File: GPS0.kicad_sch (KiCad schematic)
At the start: 12 parts, among them J2 GPS_ANT_0, U3 NEO-6M-GPS

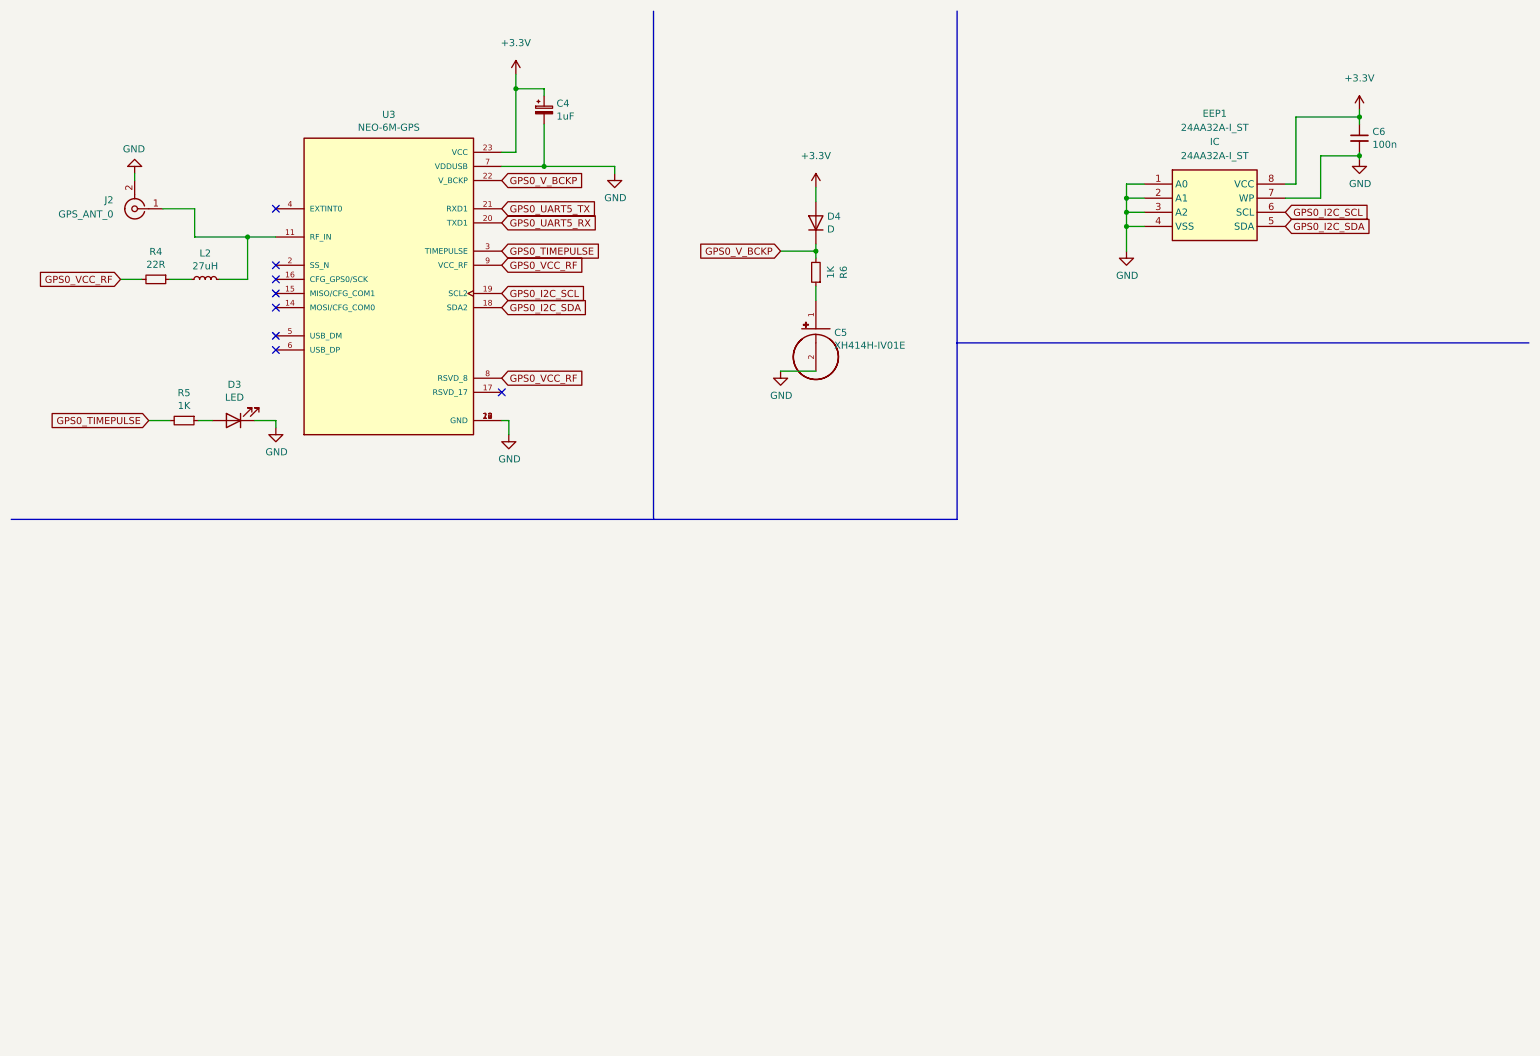
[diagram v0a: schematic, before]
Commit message: Adding M10
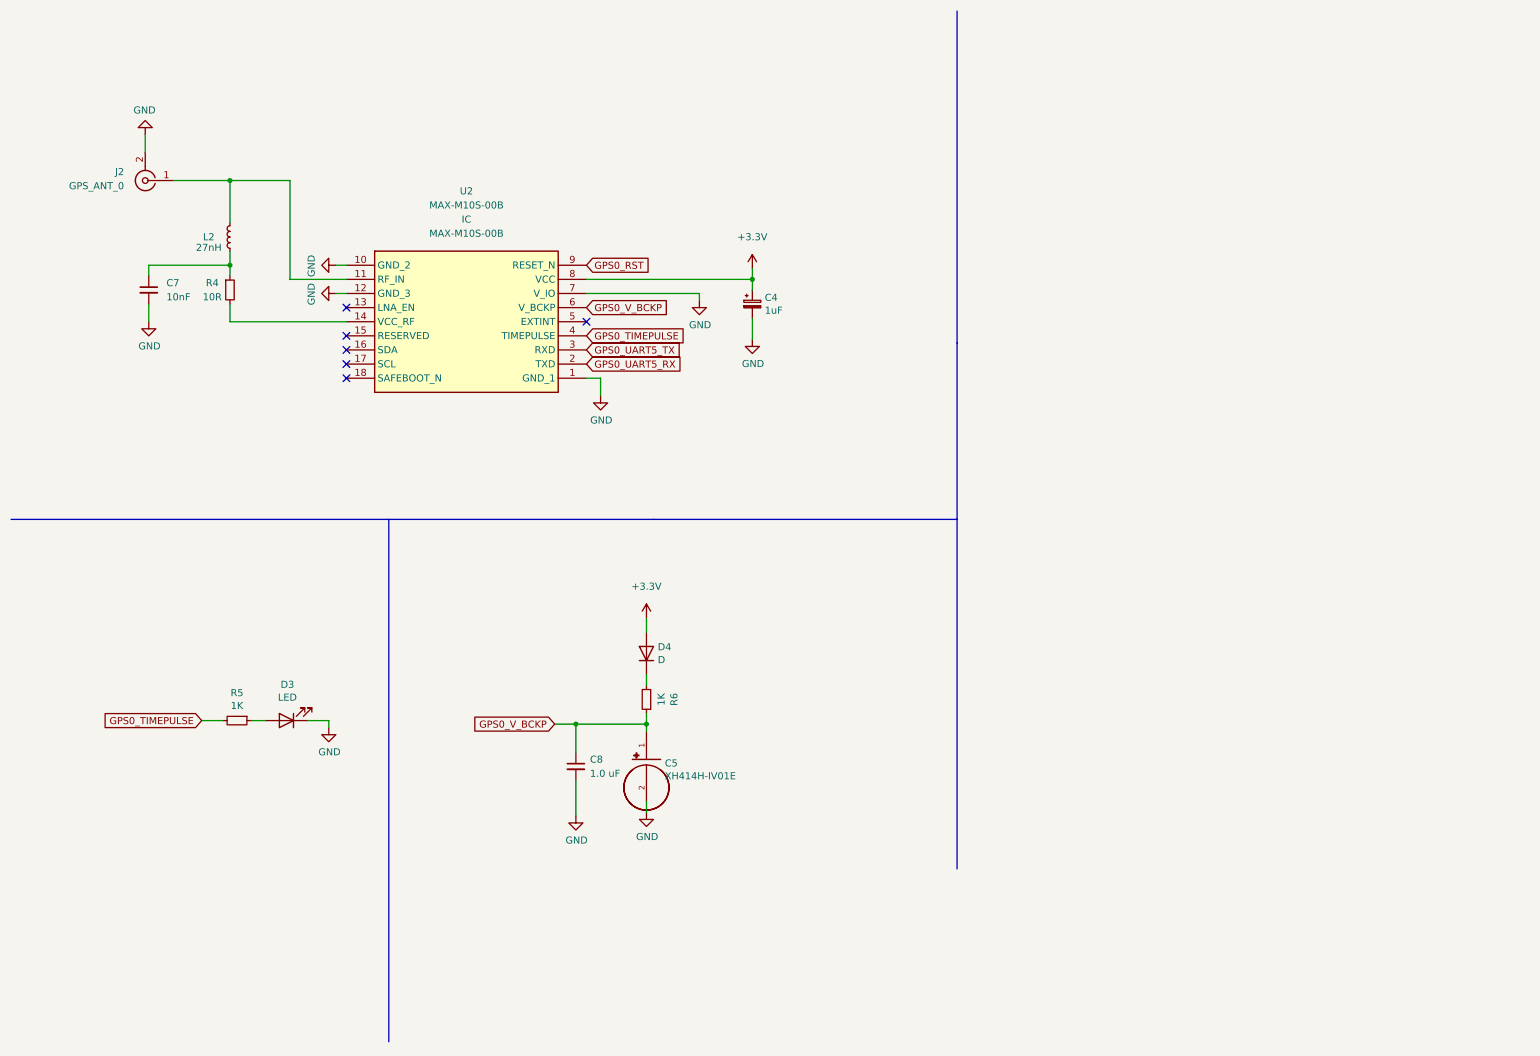
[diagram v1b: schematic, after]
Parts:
- removed C6: 100n, Capacitor_SMD:C_0402_1005Metric, symbol Device:C_Small
- removed EEP1: 24AA32A-I_ST, 24AA32A-I_ST:SOP65P640X120-8N, symbol 24AA32A-I_ST:24AA32A-I_ST
- removed U3: NEO-6M-GPS, NEO 6M:XCVR_NEO-6M-GPS, symbol NEO-6M-GPS:NEO-6M-GPS
- added C7: 10nF, Capacitor_SMD:C_0805_2012Metric, symbol Device:C_Small
- added C8: 1.0 uF, Capacitor_SMD:C_0805_2012Metric, symbol Device:C_Small
- added U2: MAX-M10S-00B, MAX-M10S-00B:MAXM10S00B, symbol MAX-M10S-00B:MAX-M10S-00B
- L2: value 27uH -> 27nH
- R4: value 22R -> 10R
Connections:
- net +3.3V: now also U2.8 (VCC)
- net GND: now also C7.2, C8.2, U2.1 (GND_1), U2.10 (GND_2), U2.12 (GND_3), U2.7 (V_IO)
- net GPS0_TIMEPULSE: now also U2.4 (TIMEPULSE)
- net GPS0_UART5_RX: now also U2.2 (TXD)
- net GPS0_UART5_TX: now also U2.3 (RXD)
- net GPS0_V_BCKP: now also C5.1, R6.1, C8.1, U2.6 (V_BCKP); no longer D4.1 (K), R6.2
- net at J2.1 (In), L2.2: now also U2.11 (RF_IN)
- net at L2.1, R4.1: now also C7.1
- net GPS0_VCC_RF: no longer names the net of R4.2
- net GPS0_VCC_RF: now also U2.14 (VCC_RF)
- new net: D4.1 (K), R6.2
- new net GPS0_RST: U2.9 (RESET_N)
- no-connect marks 8 -> 6
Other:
- moved on the sheet: C4, C5, D3, D4, J2, L2, R4, R5, R6

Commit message: Finished M10
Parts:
- C7: footprint Capacitor_SMD:C_0805_2012Metric -> Capacitor_SMD:C_0402_1005Metric
- L2: footprint Inductor_SMD:L_0805_2012Metric -> Inductor_SMD:L_0402_1005Metric
- R4: footprint Resistor_SMD:R_0805_2012Metric -> Resistor_SMD:R_0402_1005Metric
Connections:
- net GPS0_RST renamed GPS0_RESET
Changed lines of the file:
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@@
     )
   )
-  (global_label "GPS0_RST" (shape input) (at 115.57 57.785 0) (fields_autoplaced)
+  (global_label "GPS0_RESET" (shape input) (at 115.57 57.785 0) (fields_autoplaced)
     (effects (font (size 1.27 1.27)) (justify left))
-    (property "Intersheet References" "${INTERSHEET_REFS}" (id 0) (at 127.3569 57.7056 0)
+    (property "Intersheet References" "${INTERSHEET_REFS}" (id 0) (at 129.655 57.7056 0)
       (effects (font (size 1.27 1.27)) (justify left) hide)
     )
@@
     (property "Reference" "L2" (id 0) (at 47.625 52.705 0))
     (property "Value" "27nH" (id 1) (at 47.625 54.61 0))
-    (property "Footprint" "Inductor_SMD:L_0805_2012Metric" (id 2) (at 51.435 52.705 0)
+    (property "Footprint" "Inductor_SMD:L_0402_1005Metric" (id 2) (at 51.435 52.705 0)
       (effects (font (size 1.27 1.27)) hide)
     )
@@
       (effects (font (size 1.27 1.27)) (justify left))
     )
-    (property "Footprint" "Capacitor_SMD:C_0805_2012Metric" (id 2) (at 36.83 62.23 0)
+    (property "Footprint" "Capacitor_SMD:C_0402_1005Metric" (id 2) (at 36.83 62.23 0)
       (effects (font (size 1.27 1.27)) hide)
     )
@@
     (property "Reference" "R4" (id 0) (at 48.26 60.96 0))
     (property "Value" "10R" (id 1) (at 48.26 63.5 0))
-    (property "Footprint" "Resistor_SMD:R_0805_2012Metric" (id 2) (at 51.435 62.23 0)
-      (effects (font (size 1.27 1.27)) hide)
-    )
+    (property "Footprint" "Resistor_SMD:R_0402_1005Metric" (id 2) (at 51.435 62.23 0)
+      (effects (font (size 1.27 1.27)) hide)
+    )

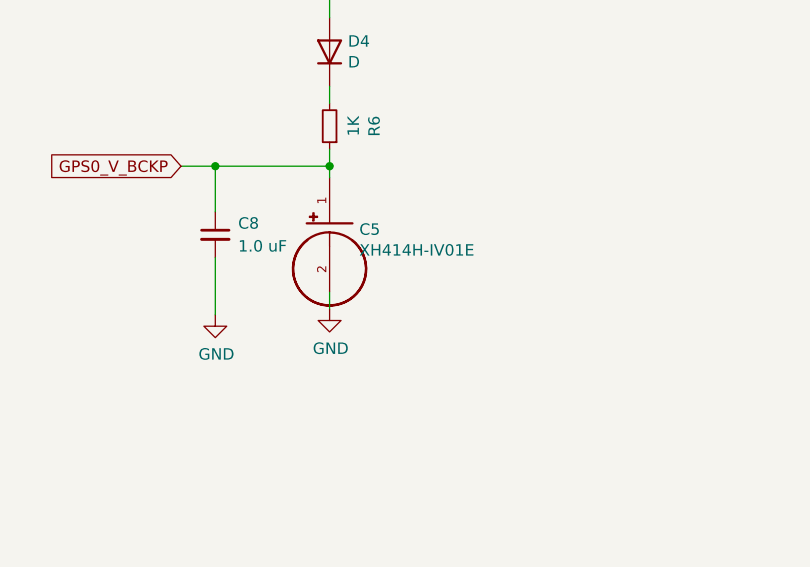
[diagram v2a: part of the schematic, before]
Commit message: Corrected battery position
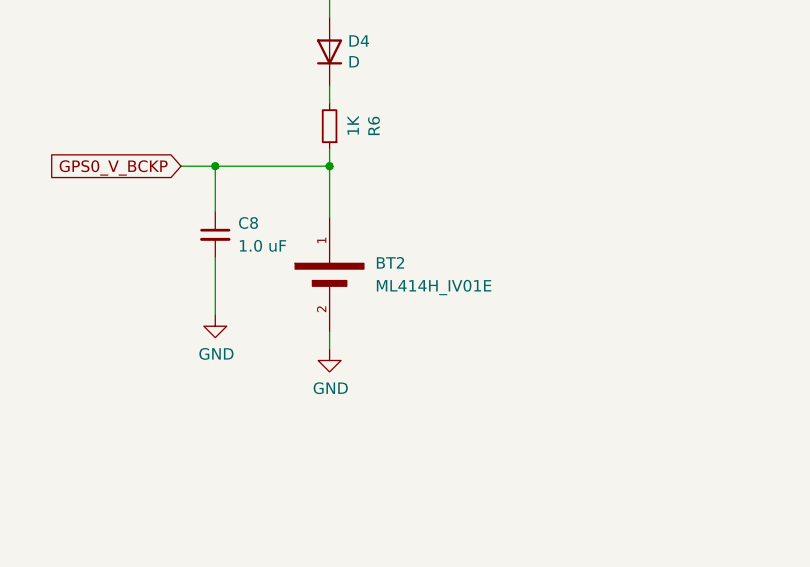
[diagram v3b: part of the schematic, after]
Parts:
- removed C5: XH414H-IV01E, XH414H:CAP_XH414H-IV01E, symbol XH414H-IV01E:XH414H-IV01E
- added BT2: ML414H_IV01E, ML414H_IV01E:SEIKO_ML414H_IV01E, symbol ML414H_IV01E:ML414H_IV01E
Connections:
- net GND: now also BT2.2
- net GPS0_V_BCKP: now also BT2.1
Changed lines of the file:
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@@
     (stroke (width 0) (type default) (color 0 0 0 0))
   )
-  (wire (pts (xy 126.365 154.305) (xy 126.365 156.21))
+  (wire (pts (xy 126.365 158.75) (xy 126.365 160.655))
     (stroke (width 0) (type default) (color 0 0 0 0))
   )
@@
     (stroke (width 0) (type default) (color 0 0 0 0))
   )
-  (wire (pts (xy 126.365 140.335) (xy 126.365 141.605))
+  (wire (pts (xy 126.365 140.335) (xy 126.365 146.05))
     (stroke (width 0) (type default) (color 0 0 0 0))
   )
@@
     (pin "2")
   )
-  (symbol (lib_id "XH414H-IV01E:XH414H-IV01E") (at 126.365 146.685 0) (unit 1)
-    (in_bom yes) (on_board yes)
-    (property "Reference" "C5" (id 0) (at 129.667 147.3708 0)
-      (effects (font (size 1.27 1.27)) (justify left))
-    )
-    (property "Value" "XH414H-IV01E" (id 1) (at 129.667 149.6822 0)
-      (effects (font (size 1.27 1.27)) (justify left))
-    )
-    (property "Footprint" "XH414H:CAP_XH414H-IV01E" (id 2) (at 126.365 146.685 0)
-      (effects (font (size 1.27 1.27)) (justify left bottom) hide)
-    )
-    (property "Datasheet" "" (id 3) (at 126.365 146.685 0)
-      (effects (font (size 1.27 1.27)) (justify left bottom) hide)
-    )
-    (property "MANUFACTURER" "Seiko" (id 4) (at 126.365 146.685 0)
-      (effects (font (size 1.27 1.27)) (justify left bottom) hide)
-    )
-    (pin "1")
-    (pin "2")
-  )
   (symbol (lib_id "Device:L_Small") (at 51.435 52.705 180) (unit 1)
     (in_bom yes) (on_board yes)
@@
     (pin "1")
   )
+  (symbol (lib_id "ML414H_IV01E:ML414H_IV01E") (at 126.365 151.13 270) (unit 1)
+    (in_bom yes) (on_board yes) (fields_autoplaced)
+    (property "Reference" "BT2" (id 0) (at 131.445 151.1299 90)
+      (effects (font (size 1.27 1.27)) (justify left))
+    )
+    (property "Value" "ML414H_IV01E" (id 1) (at 131.445 153.6699 90)
+      (effects (font (size 1.27 1.27)) (justify left))
+    )
+    (property "Footprint" "ML414H_IV01E:SEIKO_ML414H_IV01E" (id 2) (at 126.365 151.13 0)
+      (effects (font (size 1.27 1.27)) (justify bottom) hide)
+    )
+    (property "Datasheet" "" (id 3) (at 126.365 151.13 0)
+      (effects (font (size 1.27 1.27)) hide)
+    )
+    (property "STANDARD" "Manufacturer Recommendation" (id 4) (at 126.365 151.13 0)
+      (effects (font (size 1.27 1.27)) (justify bottom) hide)
+    )
+    (property "MANUFACTURER" "SEIKO" (id 5) (at 126.365 151.13 0)
+      (effects (font (size 1.27 1.27)) (justify bottom) hide)
+    )
+    (pin "1")
+    (pin "2")
+  )
   (symbol (lib_id "power:GND") (at 135.89 64.135 0) (unit 1)
     (in_bom yes) (on_board yes)
@@
     (pin "2")
   )
-  (symbol (lib_id "power:GND") (at 126.365 156.21 0) (unit 1)
-    (in_bom yes) (on_board yes)
-    (property "Reference" "#PWR023" (id 0) (at 126.365 162.56 0)
-      (effects (font (size 1.27 1.27)) hide)
-    )
-    (property "Value" "GND" (id 1) (at 126.492 160.6042 0))
-    (property "Footprint" "" (id 2) (at 126.365 156.21 0)
-      (effects (font (size 1.27 1.27)) hide)
-    )
-    (property "Datasheet" "" (id 3) (at 126.365 156.21 0)
-      (effects (font (size 1.27 1.27)) hide)
-    )
+  (symbol (lib_id "power:GND") (at 126.365 160.655 0) (unit 1)
+    (in_bom yes) (on_board yes)
+    (property "Reference" "#PWR023" (id 0) (at 126.365 167.005 0)
+      (effects (font (size 1.27 1.27)) hide)
+    )
+    (property "Value" "GND" (id 1) (at 126.492 165.0492 0))
+    (property "Footprint" "" (id 2) (at 126.365 160.655 0)
+      (effects (font (size 1.27 1.27)) hide)
+    )
+    (property "Datasheet" "" (id 3) (at 126.365 160.655 0)
+      (effects (font (size 1.27 1.27)) hide)
+    )

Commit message: Last commit
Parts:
- removed D4: D, Diode_SMD:D_1206_3216Metric_Pad1.42x1.75mm_HandSolder, symbol Device:D
- added D9: B0520LW-7-F, B0520LW-7-F:SOD3716X145N, symbol B0520LW-7-F:B0520LW-7-F
- C4: value 1uF -> 10uF; footprint Capacitor_Tantalum_SMD:CP_EIA-3528-21_Kemet-B_Pad1.50x2.35mm_HandSolder -> Capacitor_SMD:C_1210_3225Metric
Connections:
- net +3.3V: now also U2.7 (V_IO), D9.2 (A)
- net GND: no longer U2.7 (V_IO)
- net at R6.2: now also D9.1 (K)
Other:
- moved on the sheet: BT2, C4, C7, C8, J2, L2, R4, R6, U2

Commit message: Second commit
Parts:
- removed C4: 10uF, Capacitor_SMD:C_1210_3225Metric, symbol Device:CP_Small
- removed U2: MAX-M10S-00B, MAX-M10S-00B:MAXM10S00B, symbol MAX-M10S-00B:MAX-M10S-00B
- added C3: 1uF, Capacitor_SMD:C_1210_3225Metric, symbol Device:C_Small
- added C4: 100n, Capacitor_SMD:C_0402_1005Metric, symbol Device:C_Small
- added C5: 10uF, Capacitor_SMD:C_1210_3225Metric, symbol Device:C_Small
- added IC1: 24AA32A-I_ST, 24AA32A-I_ST:SOP65P640X120-8N, symbol 24AA32A-I_ST:24AA32A-I_ST
- added R7: 10K, Resistor_SMD:R_0402_1005Metric, symbol Device:R_Small
- added R8, R9: 4.7K, Resistor_SMD:R_0402_1005Metric, symbol Device:R_Small
- added U3: NEO-M9N, NEO-M9N:XCVR_NEO-M9N, symbol NEO-M9N:NEO-M9N
- BT2: footprint ML414H_IV01E:SEIKO_ML414H_IV01E -> ML414H IV01E:SEIKO_ML414H_IV01E
- C7: value 10nF -> 100nF
- J2: footprint Connector_Coaxial:SMA_Samtec_SMA-J-P-X-ST-EM1_EdgeMount -> Connector_Coaxial:SMA_Samtec_SMA-J-P-H-ST-EM1_EdgeMount
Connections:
- net +3.3V: now also C3.1, C4.1, C5.1, IC1.8 (VCC), R7.2, R8.1, R9.1, U3.23 (VCC)
- net GND: now also C3.2, C4.2, C5.2, IC1.1 (A0), IC1.2 (A1), IC1.3 (A2), IC1.4 (VSS), IC1.7 (WP), U3.10 (GND), U3.12 (GND), U3.13 (GND), U3.24 (GND)
- net GPS0_RESET: now also U3.8 (RESET_N)
- net GPS0_TIMEPULSE: now also U3.3 (TIMEPULSE)
- net GPS0_UART5_RX: now also U3.20 (TXD/SPI_MISO)
- net GPS0_UART5_TX: now also U3.21 (RXD/SPI_MOSI)
- net GPS0_V_BCKP: now also U3.22 (V_BCKP)
- net at J2.1 (In), L2.2: now also U3.11 (RF_IN)
- net GPS0_RF: now reaches R4.2
- net GPS0_RF: now also U3.9 (VCC_RF)
- new net: U3.15 (RESERVED), U3.16 (RESERVED), U3.17 (RESERVED)
- new net GPS0_D_SEL: R7.1, U3.2 (D_SEL)
- new net GPS0_I2C_SCL: IC1.6 (SCL), R9.2, U3.19 (SCL/SPI_CLK)
- new net GPS0_I2C_SDA: IC1.5 (SDA), R8.2, U3.18 (SDA/SPI_CS_N)
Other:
- moved on the sheet: BT2, C7, C8, D3, D9, J2, L2, R4, R5, R6
